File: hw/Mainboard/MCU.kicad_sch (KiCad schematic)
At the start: 73 parts, among them J12 NOT_HDMI_A, J13 Micro_SD, J14 USB2.0_HOST_TYPE_C, J15 DEBUG, J16 MCU, J17 BOOTSEL, J22 MENU, SW2 RUN, SW3 MENU, U14 RP2040, U16 W25Q128JVS, Y1 12 MHz

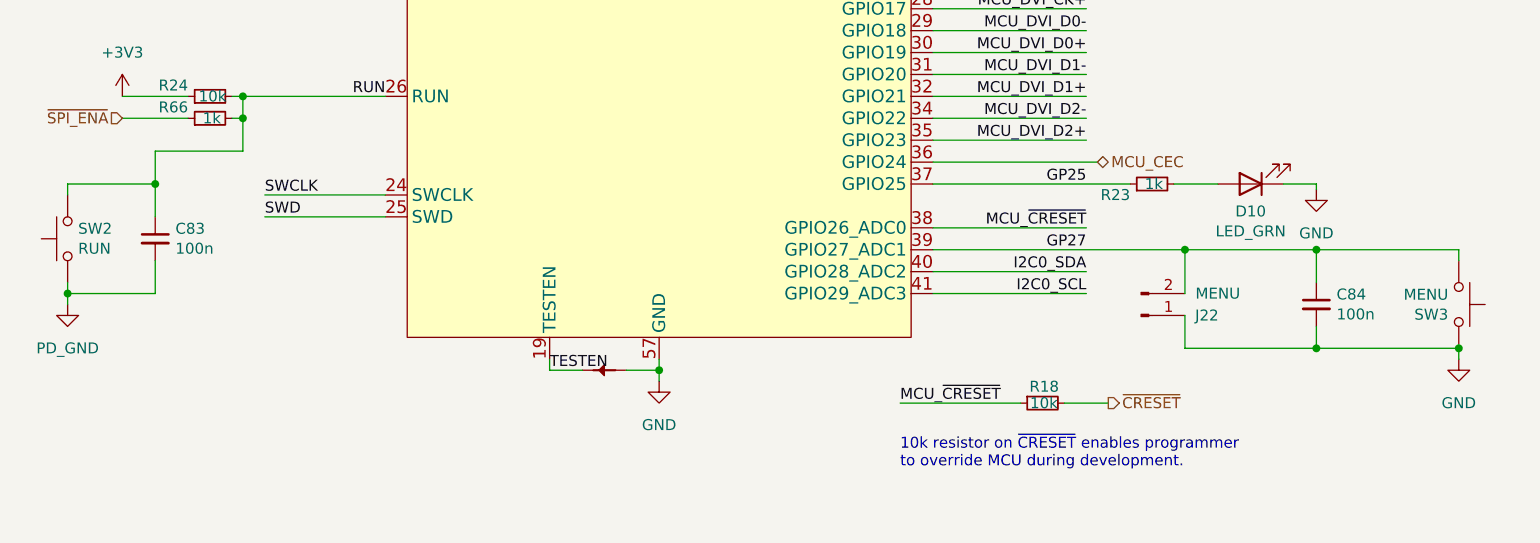
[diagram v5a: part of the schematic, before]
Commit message: hw: tidy CPU, rename RD/WR strobe to RAM_OE/_WE, debounce switches
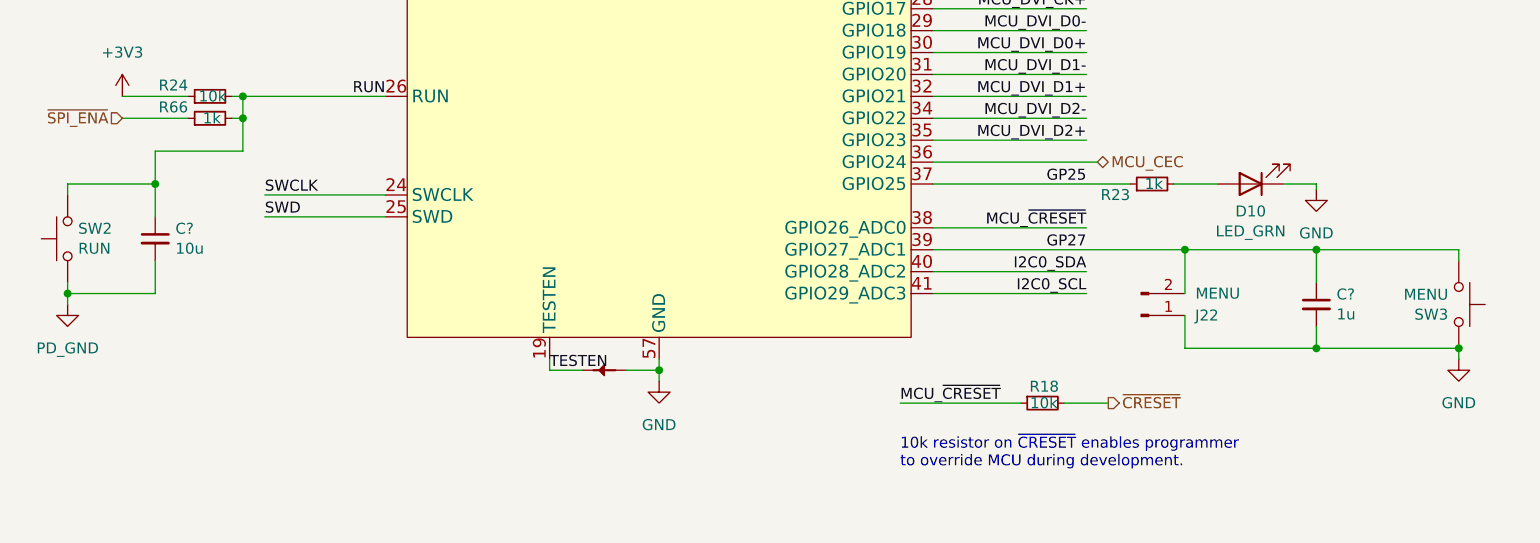
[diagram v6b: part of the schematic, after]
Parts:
- removed C83, C84: 100n, Capacitor_SMD:C_0402_1005Metric, symbol Device:C_Small
- added C?: 10u, Capacitor_SMD:C_0603_1608Metric, symbol Device:C_Small
- added C?: 1u, Capacitor_SMD:C_0402_1005Metric, symbol Device:C_Small
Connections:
- net GND: now also C?.2
- net GP27: now also C?.1
- net PD_GND: now also C?.2
- net RUN: now also C?.1
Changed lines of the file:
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@@
   (junction (at 140.97 49.53) (diameter 0) (color 0 0 0 0)
   )
-  (junction (at 102.87 148.59) (diameter 0) (color 0 0 0 0)
-  )
   (junction (at 322.58 35.56) (diameter 0) (color 0 0 0 0)
   )
@@
   (junction (at 210.82 63.5) (diameter 0) (color 0 0 0 0)
   )
+  (junction (at 102.87 148.59) (diameter 0) (color 0 0 0 0)
+  )
   (junction (at 152.4 66.04) (diameter 0) (color 0 0 0 0)
   )
@@
     (stroke (width 0) (type default) (color 0 0 0 0))
   )
+  (wire (pts (xy 102.87 148.59) (xy 102.87 152.4))
+    (stroke (width 0) (type default) (color 0 0 0 0))
+  )
   (wire (pts (xy 210.82 55.88) (xy 219.71 55.88))
     (stroke (width 0) (type default) (color 0 0 0 0))
@@
     (stroke (width 0) (type default) (color 0 0 0 0))
   )
+  (wire (pts (xy 102.87 157.48) (xy 102.87 161.29))
+    (stroke (width 0) (type default) (color 0 0 0 0))
+  )
   (wire (pts (xy 36.83 252.73) (xy 36.83 254))
     (stroke (width 0) (type default) (color 0 0 0 0))
@@
     (stroke (width 0) (type default) (color 0 0 0 0))
   )
-  (wire (pts (xy 102.87 148.59) (xy 102.87 152.4))
-    (stroke (width 0) (type default) (color 0 0 0 0))
-  )
   (wire (pts (xy 257.81 214.63) (xy 257.81 213.36))
     (stroke (width 0) (type default) (color 0 0 0 0))
@@
     (stroke (width 0) (type default) (color 0 0 0 0))
   )
-  (wire (pts (xy 102.87 161.29) (xy 102.87 157.48))
-    (stroke (width 0) (type default) (color 0 0 0 0))
-  )
   (wire (pts (xy 161.29 170.18) (xy 161.29 171.45))
     (stroke (width 0) (type default) (color 0 0 0 0))
@@
     (pin "2")
   )
+  (symbol (lib_id "Device:C_Small") (at 102.87 154.94 0) (unit 1)
+    (in_bom yes) (on_board yes)
+    (property "Reference" "C?" (id 0) (at 105.2068 153.7716 0)
+      (effects (font (size 1.27 1.27)) (justify left))
+    )
+    (property "Value" "10u" (id 1) (at 105.2068 156.083 0)
+      (effects (font (size 1.27 1.27)) (justify left))
+    )
+    (property "Footprint" "Capacitor_SMD:C_0603_1608Metric" (id 2) (at 102.87 154.94 0)
+      (effects (font (size 1.27 1.27)) hide)
+    )
+    (property "Datasheet" "" (id 3) (at 102.87 154.94 0)
+      (effects (font (size 1.27 1.27)) hide)
+    )
+    (property "LCSC" "C96446" (id 4) (at 102.87 154.94 0)
+      (effects (font (size 1.27 1.27)) hide)
+    )
+    (pin "1")
+    (pin "2")
+  )
   (symbol (lib_id "Device:R_Small") (at 311.15 162.56 0) (unit 1)
     (in_bom yes) (on_board yes)
@@
     (pin "2")
   )
-  (symbol (lib_id "Device:C_Small") (at 102.87 154.94 0) (unit 1)
-    (in_bom yes) (on_board yes)
-    (property "Reference" "C83" (id 0) (at 105.2068 153.7716 0)
-      (effects (font (size 1.27 1.27)) (justify left))
-    )
-    (property "Value" "100n" (id 1) (at 105.2068 156.083 0)
-      (effects (font (size 1.27 1.27)) (justify left))
-    )
-    (property "Footprint" "Capacitor_SMD:C_0402_1005Metric" (id 2) (at 102.87 154.94 0)
-      (effects (font (size 1.27 1.27)) hide)
-    )
-    (property "Datasheet" "https://datasheet.lcsc.com/lcsc/1810191219_Samsung-Electro-Mechanics-CL05B104KO5NNNC_C1525.pdf" (id 3) (at 102.87 154.94 0)
-      (effects (font (size 1.27 1.27)) hide)
-    )
-    (property "LCSC" "C1525" (id 4) (at 102.87 154.94 0)
-      (effects (font (size 1.27 1.27)) hide)
-    )
-    (pin "1")
-    (pin "2")
-  )
   (symbol (lib_id "PET:PowerTie_2") (at 377.19 93.98 0) (mirror y) (unit 1)
     (in_bom yes) (on_board yes)
@@
     (pin "1")
   )
-  (symbol (lib_id "Device:C_Small") (at 237.49 162.56 0) (unit 1)
-    (in_bom yes) (on_board yes)
-    (property "Reference" "C84" (id 0) (at 239.8268 161.3916 0)
-      (effects (font (size 1.27 1.27)) (justify left))
-    )
-    (property "Value" "100n" (id 1) (at 239.8268 163.703 0)
-      (effects (font (size 1.27 1.27)) (justify left))
-    )
-    (property "Footprint" "Capacitor_SMD:C_0402_1005Metric" (id 2) (at 237.49 162.56 0)
-      (effects (font (size 1.27 1.27)) hide)
-    )
-    (property "Datasheet" "https://datasheet.lcsc.com/lcsc/1810191219_Samsung-Electro-Mechanics-CL05B104KO5NNNC_C1525.pdf" (id 3) (at 237.49 162.56 0)
-      (effects (font (size 1.27 1.27)) hide)
-    )
-    (property "LCSC" "C1525" (id 4) (at 237.49 162.56 0)
-      (effects (font (size 1.27 1.27)) hide)
-    )
-    (pin "1")
-    (pin "2")
-  )
   (symbol (lib_id "Device:R_Small") (at 322.58 162.56 0) (unit 1)
     (in_bom yes) (on_board yes)
@@
     (pin "1")
   )
+  (symbol (lib_id "Device:C_Small") (at 237.49 162.56 0) (unit 1)
+    (in_bom yes) (on_board yes)
+    (property "Reference" "C?" (id 0) (at 239.8268 161.3916 0)
+      (effects (font (size 1.27 1.27)) (justify left))
+    )
+    (property "Value" "1u" (id 1) (at 239.8268 163.703 0)
+      (effects (font (size 1.27 1.27)) (justify left))
+    )
+    (property "Footprint" "Capacitor_SMD:C_0402_1005Metric" (id 2) (at 237.49 162.56 0)
+      (effects (font (size 1.27 1.27)) hide)
+    )
+    (property "Datasheet" "https://datasheet.lcsc.com/lcsc/1811091611_Samsung-Electro-Mechanics-CL05A105KA5NQNC_C52923.pdf" (id 3) (at 237.49 162.56 0)
+      (effects (font (size 1.27 1.27)) hide)
+    )
+    (property "LCSC" "C52923" (id 4) (at 237.49 162.56 0)
+      (effects (font (size 1.27 1.27)) hide)
+    )
+    (pin "1")
+    (pin "2")
+  )
   (symbol (lib_id "power:GND") (at 153.67 232.41 0) (unit 1)

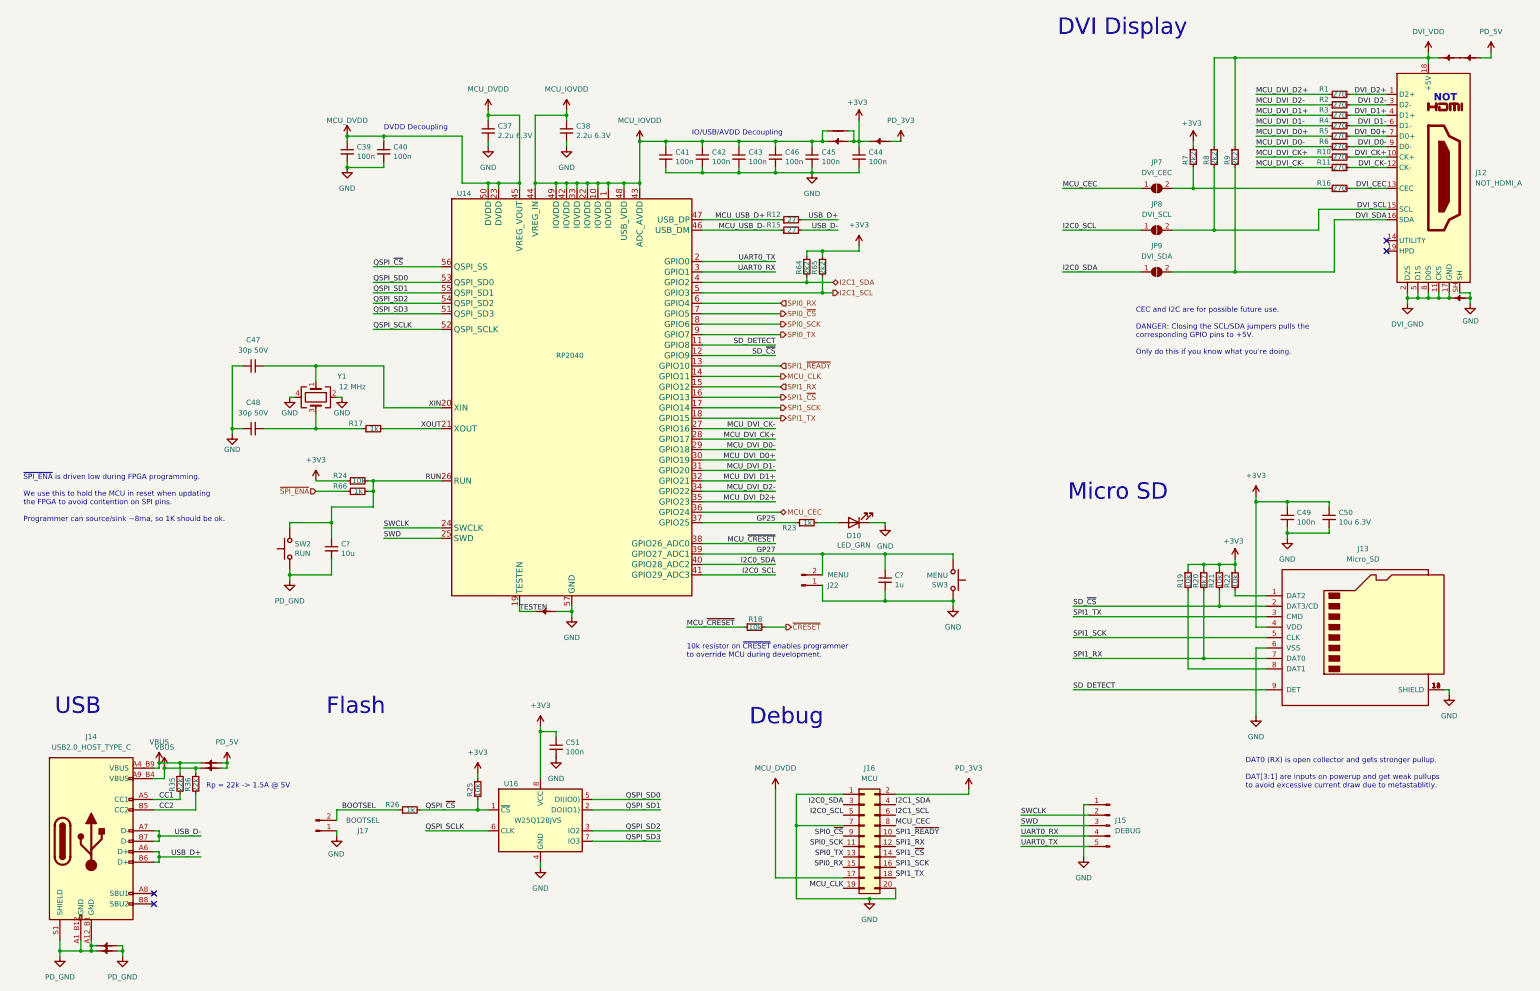
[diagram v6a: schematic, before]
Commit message: hw: tidy MCU and a few missed PD_
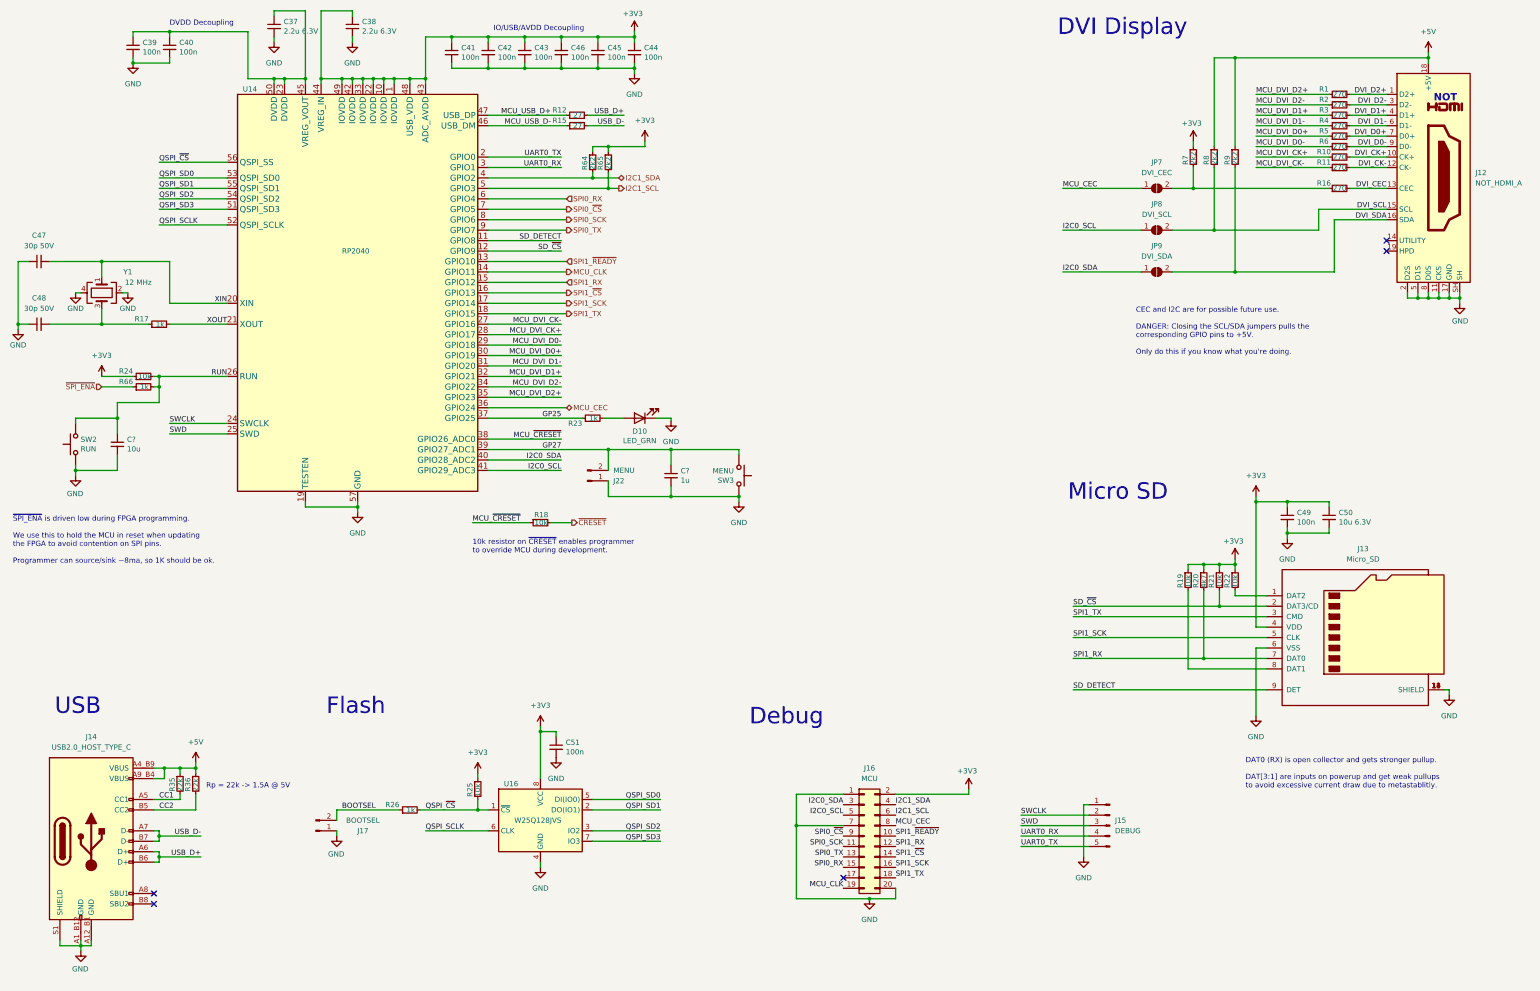
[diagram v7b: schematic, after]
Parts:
- removed NT18, NT20, NT37, NT38: +5V, PET:NetTie-2_SMD_Pad_1.6_to_0.4mm, symbol PET:PowerTie_2
- removed NT19, NT21: GND, PET:NetTie-2_SMD_Pad_1.6_to_0.4mm, symbol PET:PowerTie_2
- removed NT3, NT5: +3V3, PET:NetTie-2_SMD_Pad_0.4_to_0.2mm, symbol PET:PowerTie_2
- removed NT4: GND, PET:NetTie-2_SMD_Pad_0.4_to_0.2mm, symbol PET:PowerTie_2
- removed NT41: +3V3, PET:NetTie-2_SMD_Pad_0.4_to_0.2mm, symbol Device:NetTie_2
- removed NT6: +5V, PET:NetTie-2_SMD_Pad_0.4_to_0.28mm, symbol PET:PowerTie_2
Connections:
- net DVI_GND is gone; now on net GND: J12.11 (CKS), J12.17 (GND), J12.2 (D2S), J12.5 (D1S), J12.8 (D0S)
- net MCU_IOVDD is gone; now on net +3V3: C38.1, C41.1, C42.1, C43.1, C45.1, C46.1, U14.1 (IOVDD), U14.10 (IOVDD), U14.22 (IOVDD), U14.33 (IOVDD), U14.42 (IOVDD), U14.43 (ADC_AVDD), U14.44 (VREG_IN), U14.48 (USB_VDD), U14.49 (IOVDD)
- net PD_3V3 is gone; now on net +3V3: J16.2 (Pin_2)
- net PD_GND is gone; now on net GND: C?.2, J14.A12_B1 (GND), J14.A1_B12 (GND), J14.S1 (SHIELD), SW2.1
- net TESTEN is gone; now on net GND: U14.19 (TESTEN)
- net VBUS is gone; now on net +5V: J14.A4_B9 (VBUS), J14.A9_B4 (VBUS), R35.1, R36.1
- net DVI_VDD renamed +5V
- net MCU_DVDD: no longer names the net of C37.1, C39.1, C40.1, U14.23 (DVDD), U14.45 (VREG_VOUT), U14.50 (DVDD)
- net MCU_DVDD: no longer J16.17 (Pin_17)
- no-connect marks 4 -> 5
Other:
- moved on the sheet: C37, C38, C39, C40, C41, C42, C43, C44, C45, C46, C47, C48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

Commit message: hw: move DVI to separate hierarchical sheet, fix buses, annotate power
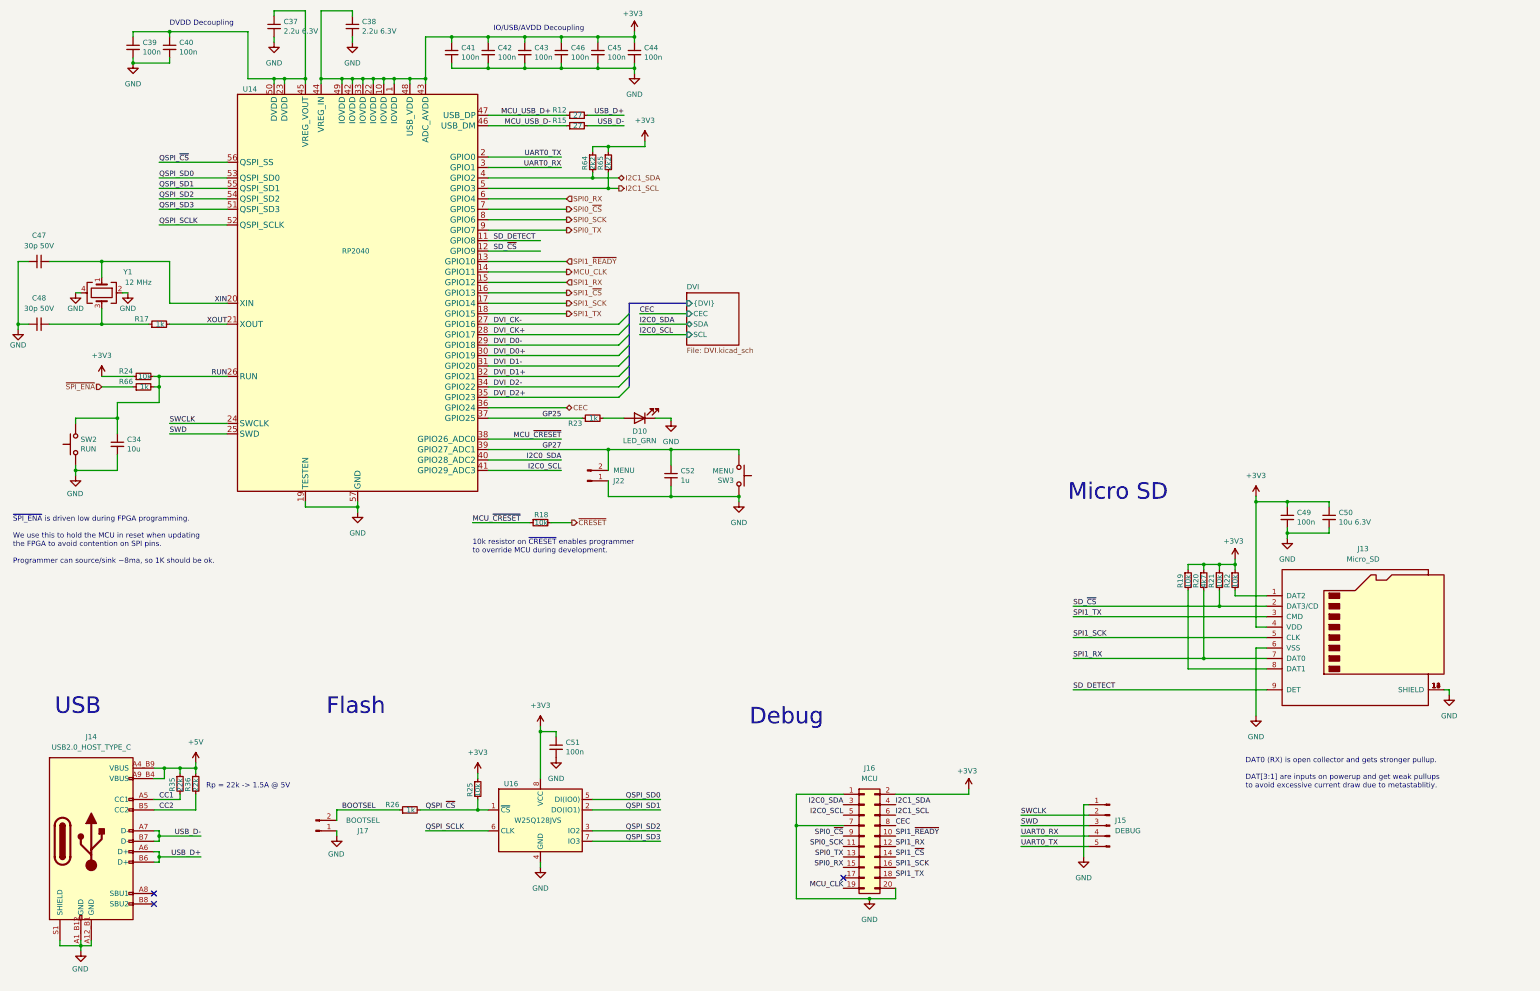
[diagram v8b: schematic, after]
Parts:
- removed J12: NOT_HDMI_A, Connector_HDMI:HDMI_A_Molex_208658-1001_Horizontal, symbol Connector:HDMI_A
- removed JP7: DVI_CEC, Jumper:SolderJumper-2_P1.3mm_Open_RoundedPad1.0x1.5mm, symbol Jumper:SolderJumper_2_Open
- removed JP8: DVI_SCL, Jumper:SolderJumper-2_P1.3mm_Open_RoundedPad1.0x1.5mm, symbol Jumper:SolderJumper_2_Open
- removed JP9: DVI_SDA, Jumper:SolderJumper-2_P1.3mm_Open_RoundedPad1.0x1.5mm, symbol Jumper:SolderJumper_2_Open
- removed R1, R10, R11, R16, R2, R3, R4, R5, R6: 270, Resistor_SMD:R_0603_1608Metric, symbol Device:R_Small
- removed R7, R8, R9: 2k2, Resistor_SMD:R_0402_1005Metric, symbol Device:R_Small
- gave numbers to parts that had none: 2
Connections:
- net MCU_DVI_CK+ is gone; now on net DVI_CK+: U14.28 (GPIO17)
- net MCU_DVI_CK- is gone; now on net DVI_CK-: U14.27 (GPIO16)
- net MCU_DVI_D0+ is gone; now on net DVI_D0+: U14.30 (GPIO19)
- net MCU_DVI_D0- is gone; now on net DVI_D0-: U14.29 (GPIO18)
- net MCU_DVI_D1+ is gone; now on net DVI_D1+: U14.32 (GPIO21)
- net MCU_DVI_D1- is gone; now on net DVI_D1-: U14.31 (GPIO20)
- net MCU_DVI_D2+ is gone; now on net DVI_D2+: U14.35 (GPIO23)
- net MCU_DVI_D2- is gone; now on net DVI_D2-: U14.34 (GPIO22)
- net MCU_CEC renamed CEC
- no-connect marks 5 -> 3
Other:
- added sheet DVI (DVI.kicad_sch)
- note removed: "CEC and I2C are for possible future use. DANGER: Closing the SCL/SDA jumpers pulls the corresponding GPIO pins to +5V. Only do this if you know what you're doing."
- note removed: "DVI Display"
- note removed: "NOT"
